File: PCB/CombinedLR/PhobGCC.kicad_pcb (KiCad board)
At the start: 2 copper layers, 147.6 x 91.4 mm, 82 parts, among them J1 Conn_01x06_Female, J2 Conn_01x04_Female, J3 Conn_01x01_Male, J4 Conn_01x04_Male, J5 Rumble, J6 L, J7 R, Q1 Q_NMOS_GSD, Q2 Q_PMOS_GDS, Q3 Q_NMOS_GSD, SW1 A, SW10 Dup, SW11 Dright, SW12 Ddown, SW13 L, SW14 R, SW2 B, SW3 X, SW4 Y, SW5 Start, SW6 L, SW7 R, SW8 Z, SW9 Dleft, U1 Teensy4.0, U2 2x DRV5053CAQLPGM Hall Effect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, U3 GP2S60-MFG, U4 GP2S60-MFG, U5 Stickbox_Assembly

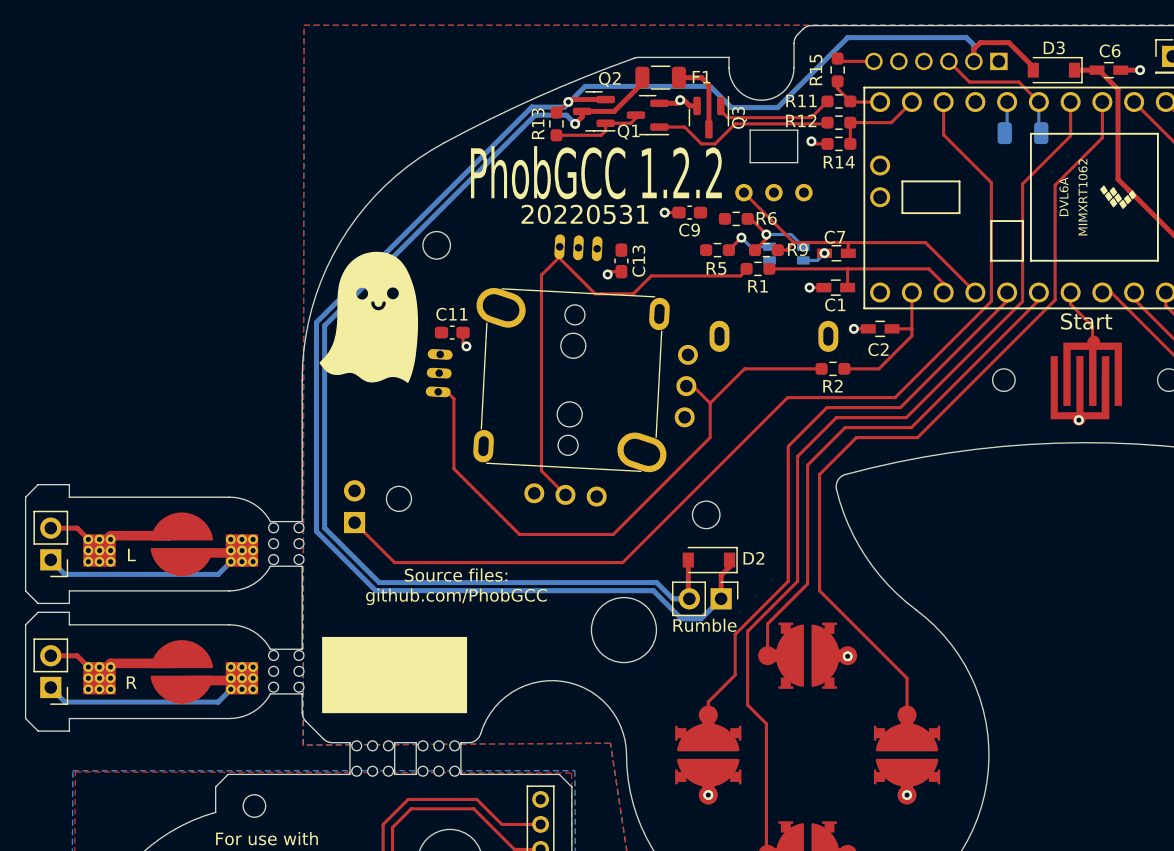
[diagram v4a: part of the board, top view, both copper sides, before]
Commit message: wide mousebites
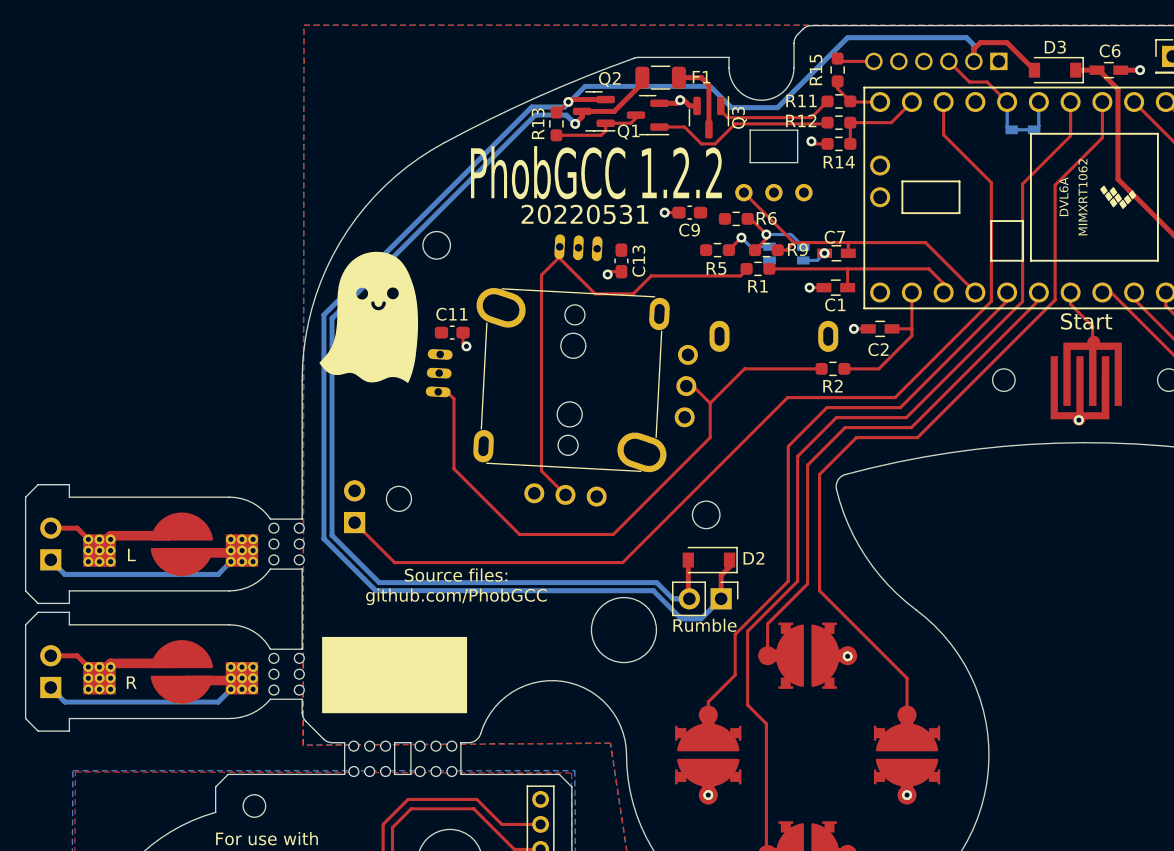
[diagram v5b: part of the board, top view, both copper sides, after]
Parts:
- removed F2: Fuse, Resistor_SMD:R_1206_3216Metric
- added D1: D_Schottky_Shorted, wavbrd:D_SOD-523_Shorted, B.Cu at (107.5, 58.4)
- J6, J7: moved to B.Cu
- moved H17 0.20 mm to (49.9, 91.3)
- moved D3 0.10 mm to (110.1, 53.6)
- turned J6 to 0 degrees
- turned J7 to 0 degrees
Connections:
- U1 pad 9: Net-(U1-Pad9) -> /Data
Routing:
- net Net-(U1-Pad9): track 2.57 -> 0.00 mm
- net /Data: track 11.1 -> 12.5 mm
- net +5V: track 132.4 -> 131.8 mm
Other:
- outline, holes or cut-outs redrawn

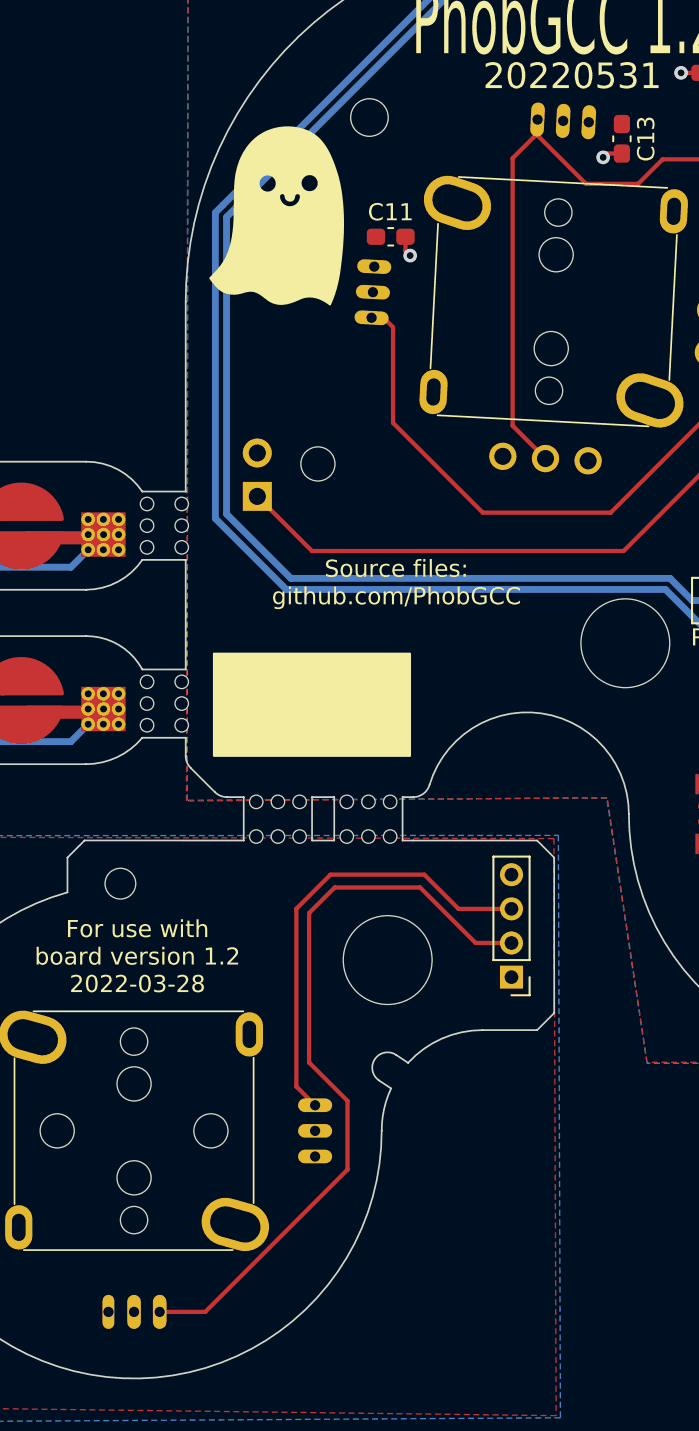
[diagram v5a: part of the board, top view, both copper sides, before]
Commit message: fixed footprints
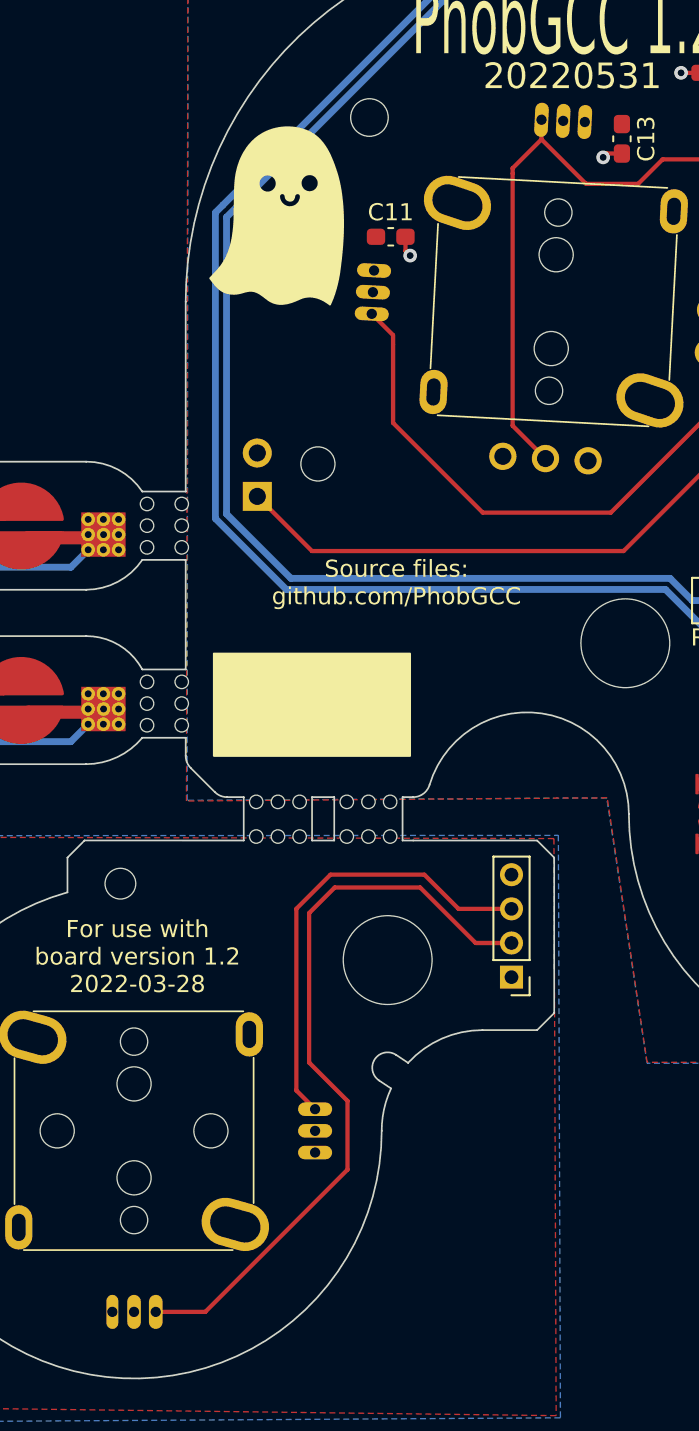
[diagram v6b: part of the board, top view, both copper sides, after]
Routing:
- net /Stick_y: track 47.1 -> 47.6 mm

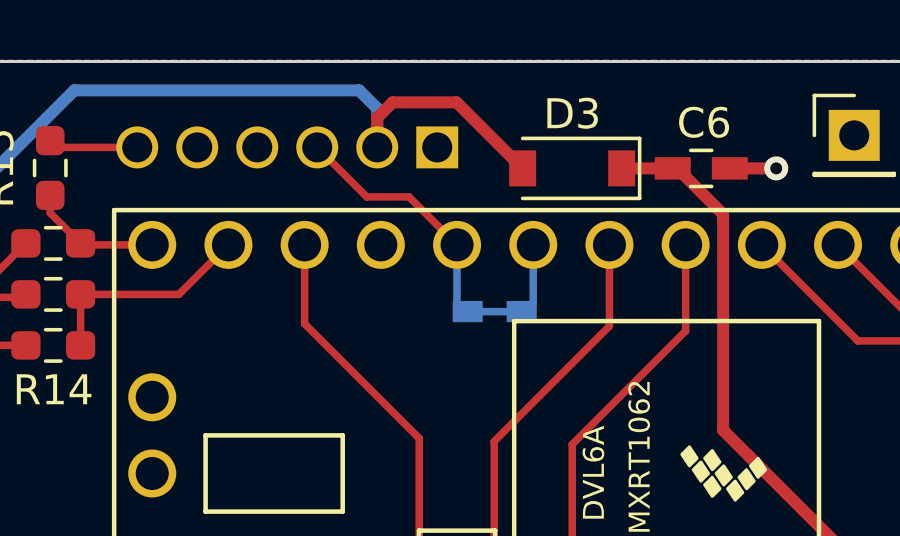
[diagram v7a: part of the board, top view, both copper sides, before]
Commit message: fixed data line connection.
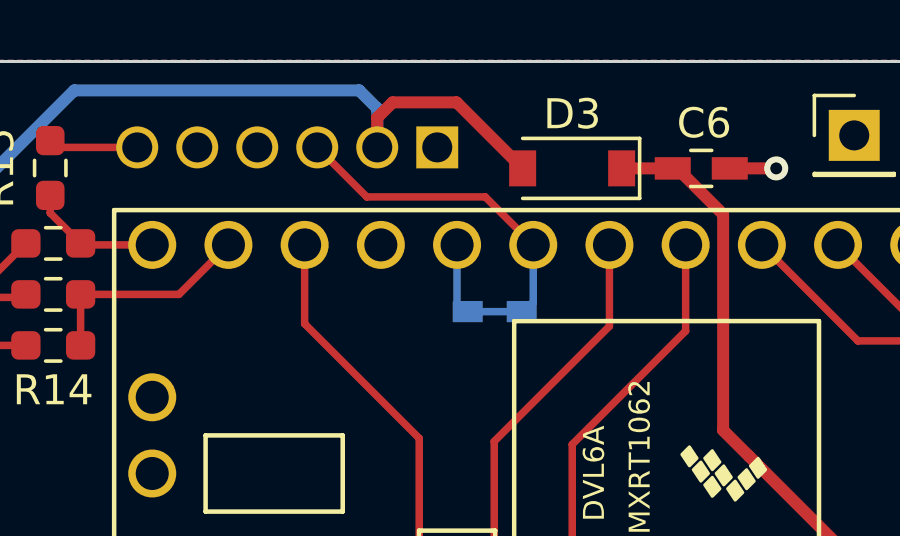
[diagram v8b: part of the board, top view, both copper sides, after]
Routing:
- net /Data: track 12.5 -> 15.0 mm
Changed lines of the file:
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@@
   (segment (start 52.247 73.453) (end 52.862 72.838) (width 0.4) (layer "B.Cu") (net 39))
   (segment (start 56.01856 94.6) (end 78.21856 94.6) (width 0.4) (layer "B.Cu") (net 39))
-  (segment (start 104.66 54.55) (end 103.25 54.55) (width 0.25) (layer "F.Cu") (net 40))
   (segment (start 101.6 52.9) (end 103.25 54.55) (width 0.25) (layer "F.Cu") (net 40))
-  (segment (start 106.26 56.15) (end 104.66 54.55) (width 0.25) (layer "F.Cu") (net 40))
+  (segment (start 103.25 54.55) (end 107.2 54.55) (width 0.25) (layer "F.Cu") (net 40))
+  (segment (start 107.2 54.55) (end 108.8 56.15) (width 0.25) (layer "F.Cu") (net 40))
   (segment (start 106.617 58.375) (end 108.417 58.375) (width 0.25) (layer "B.Cu") (net 40))
   (segment (start 106.26 58.09252) (end 106.54248 58.375) (width 0.25) (layer "B.Cu") (net 40))
